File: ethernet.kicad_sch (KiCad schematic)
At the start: 44 parts, among them J6 Bus_RJ45_5-2337992-8, Q17 PJE138K, U22 TPS2372-3RGWR, U23 ULS-12/5-D48N-C, U39 ACPL-217-500E

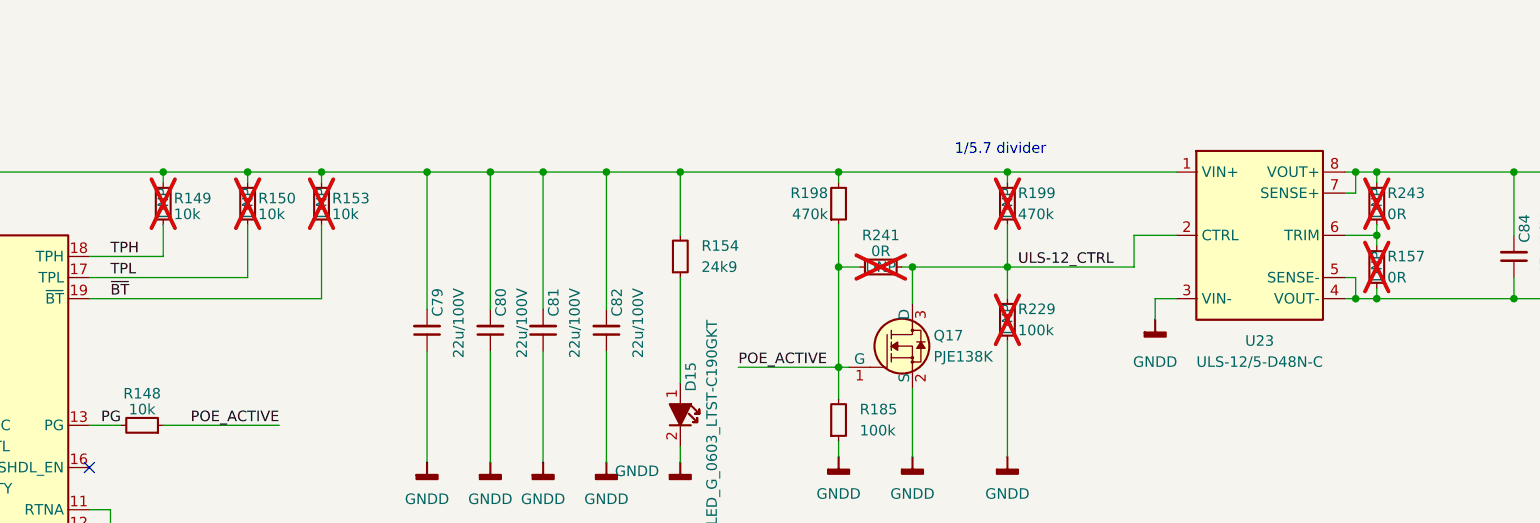
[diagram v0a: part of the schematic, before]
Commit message: 5/16 Commit: Sch Mods added and beginning Development on PCB layout
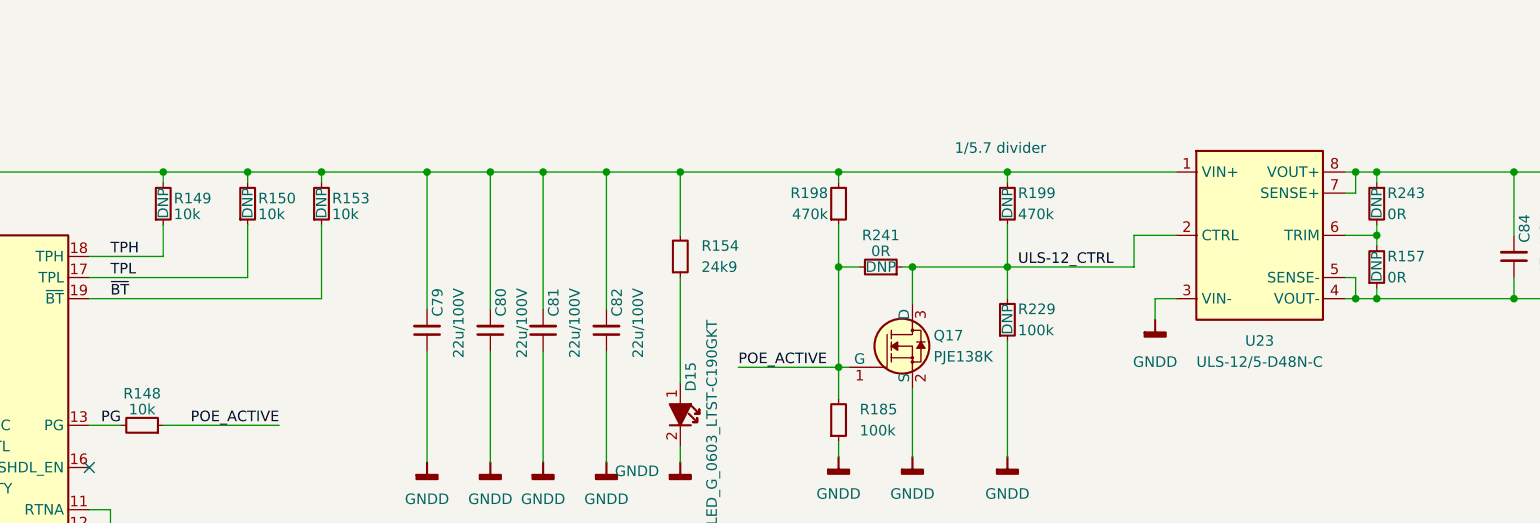
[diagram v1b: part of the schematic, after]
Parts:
- R149, R150, R153, R157, R199, R229, R241, R243: now fitted
